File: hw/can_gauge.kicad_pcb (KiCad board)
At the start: 2 copper layers, 28 parts, among them J1 Gauge 1, J2 Gauge 2, J3 Gauge 3, J4 Gauge 4, J5 Gauge 5, J6 Gauge 6, J7 Power & CAN, U1 PIC16F1459-IP, U4 74HC595, U5 74HC595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

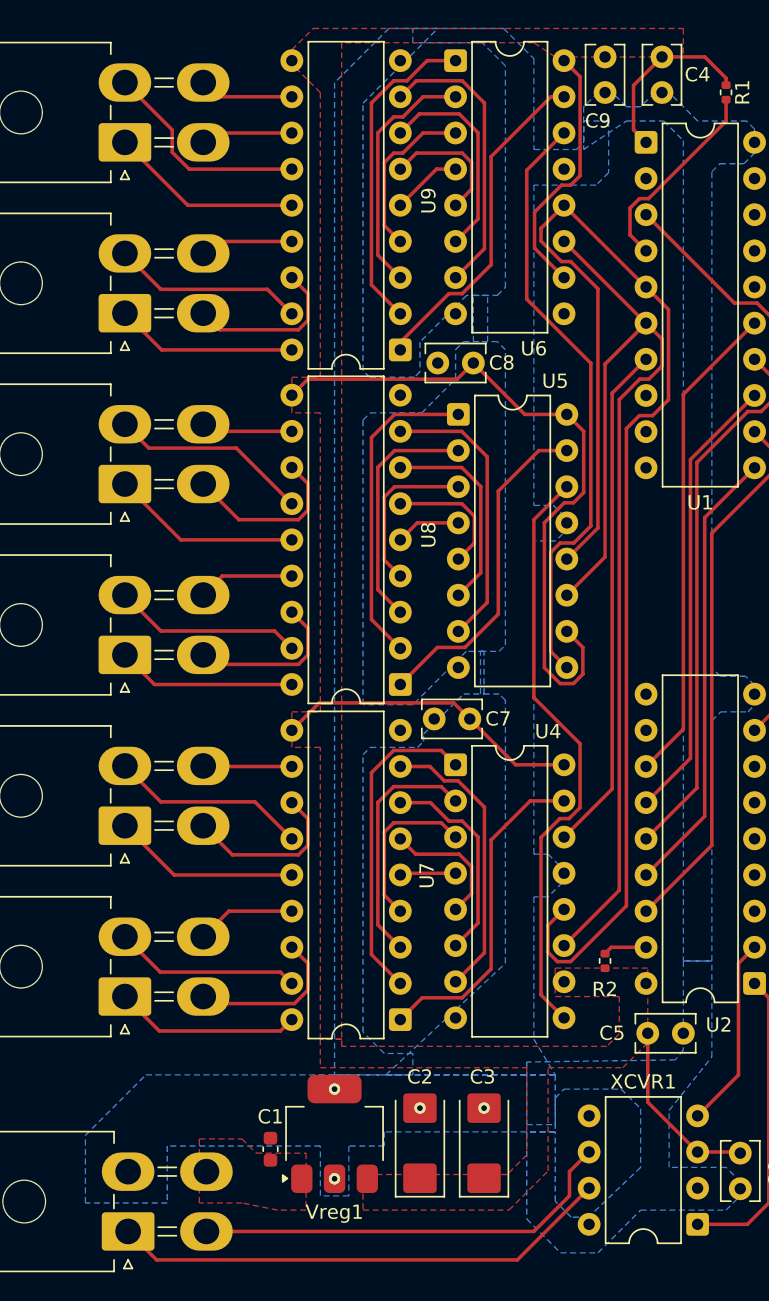
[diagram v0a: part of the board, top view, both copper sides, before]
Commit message: hw: power supply vias
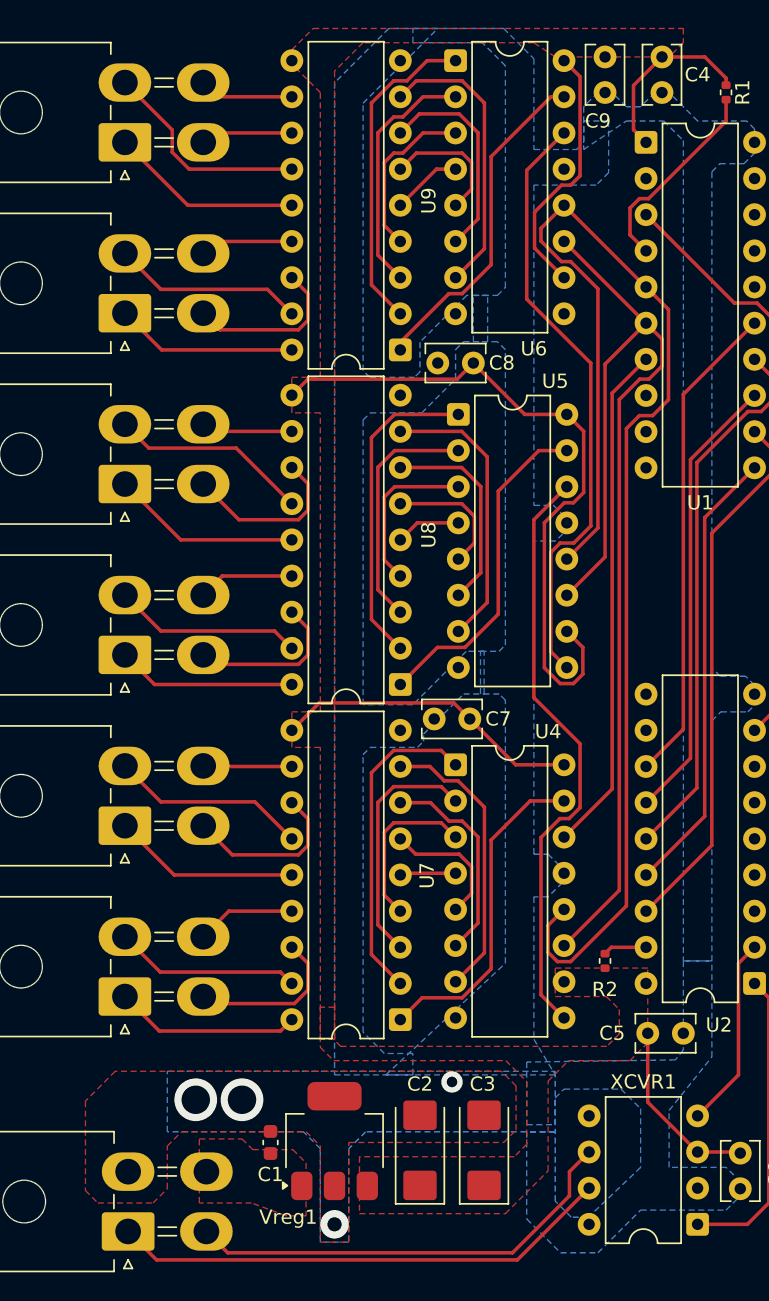
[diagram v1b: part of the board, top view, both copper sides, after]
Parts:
- moved C2 0.50 mm to (73.0, 150.3)
- moved C3 0.50 mm to (77.5, 150.3)
- moved Vreg1 0.50 mm to (67.0, 149.7)
- moved C1 0.47 mm to (62.5, 149.8)
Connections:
- Vreg1 pad 4: (no net) -> GND
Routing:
- net CAN_L: track 30.2 -> 31.4 mm
- added copper zone on F.Cu, net GND
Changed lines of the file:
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@@
 	(footprint "Package_TO_SOT_SMD:SOT-223"
 		(layer "F.Cu")
-		(at 67 149.15 90)
+		(at 67 149.65 90)
 		(descr "module CMS SOT223 4 pins")
 		(tags "CMS SOT")
 		(property "Reference" "Vreg1"
-			(at -5.5 0 0)
+			(at -5.35 -3.25 0)
 			(layer "F.SilkS")
 			(effects
@@
 			(layers "F.Cu" "F.Mask" "F.Paste")
 			(roundrect_rratio 0.25)
+			(net 1 "GND")
 		)
 		(embedded_fonts no)
@@
 	(footprint "Capacitor_SMD:C_0603_1608Metric"
 		(layer "F.Cu")
-		(at 62.5 150.225 90)
+		(at 62.5 149.75 90)
 		(descr "Capacitor SMD 0603 (1608 Metric), square (rectangular) end terminal, IPC_7351 nominal, (Body size source: IPC-SM-782 page 76, https://www.pcb-3d.com/wordpress/wp-content/uploads/ipc-sm-782a_amendment_1_and_2.pdf), generated with kicad-footprint-generator")
 		(tags "capacitor")
 		(property "Reference" "C1"
-			(at 2.275 0 180)
+			(at -2.25 0 180)
 			(layer "F.SilkS")
 			(effects
@@
 	(footprint "Capacitor_Tantalum_SMD:CP_EIA-6032-28_Kemet-C"
 		(layer "F.Cu")
-		(at 77.5 149.8 90)
+		(at 77.5 150.3 90)
 		(descr "Tantalum Capacitor SMD Kemet-C (6032-28 Metric), IPC_7351 nominal, (Body size from: http://www.kemet.com/Lists/ProductCatalog/Attachments/253/KEM_TC101_STD.pdf), generated with kicad-footprint-generator")
 		(tags "capacitor tantalum")
@@
 	(footprint "Capacitor_Tantalum_SMD:CP_EIA-6032-28_Kemet-C"
 		(layer "F.Cu")
-		(at 73 149.8 90)
+		(at 73 150.3 90)
 		(descr "Tantalum Capacitor SMD Kemet-C (6032-28 Metric), IPC_7351 nominal, (Body size from: http://www.kemet.com/Lists/ProductCatalog/Attachments/253/KEM_TC101_STD.pdf), generated with kicad-footprint-generator")
 		(tags "capacitor tantalum")
@@
 	)
 	(via
-		(at 77.5 147.3375)
-		(size 0.8)
-		(drill 0.4)
+		(at 57.25 146.75)
+		(size 3)
+		(drill 2)
 		(layers "F.Cu" "B.Cu")
+		(free yes)
 		(net 1)
 	)
 	(via
-		(at 67 152.3)
-		(size 0.8)
-		(drill 0.4)
+		(at 67 155.5)
+		(size 2)
+		(drill 1)
 		(layers "F.Cu" "B.Cu")
+		(free yes)
 		(net 1)
 	)
 	(via
-		(at 83.315 106.23)
-		(size 0.8)
-		(drill 0.4)
+		(at 60.5 146.75)
+		(size 3)
+		(drill 2)
 		(layers "F.Cu" "B.Cu")
+		(free yes)
 		(net 1)
 	)
 	(via
-		(at 67 146)
+		(at 83.315 106.23)
 		(size 0.8)
 		(drill 0.4)
 		(layers "F.Cu" "B.Cu")
-		(free yes)
 		(net 1)
 	)
 	(via
-		(at 73 147.3375)
-		(size 0.8)
-		(drill 0.4)
+		(at 75.25 145.5)
+		(size 1.5)
+		(drill 0.75)
 		(layers "F.Cu" "B.Cu")
+		(free yes)
 		(net 1)
 	)
@@
 	)
 	(segment
-		(start 58 156)
-		(end 81 156)
-		(width 0.25)
-		(layer "F.Cu")
-		(net 29)
-	)
-	(segment
-		(start 81 156)
+		(start 79.5 157.5)
 		(end 83.5 153.5)
 		(width 0.25)
@@
 	)
 	(segment
+		(start 58 156)
+		(end 59.5 157.5)
+		(width 0.25)
+		(layer "F.Cu")
+		(net 29)
+	)
+	(segment
+		(start 59.5 157.5)
+		(end 79.5 157.5)
+		(width 0.25)
+		(layer "F.Cu")
+		(net 29)
+	)
+	(segment
 		(start 88.413595 83.454)
 		(end 89.058405 83.454)
@@
 		(polygon
 			(pts
-				(xy 57.5 149.5) (xy 60.5 149.5) (xy 61.5 150.5) (xy 63.5 150.5) (xy 65 150.5) (xy 65 154.5) (xy 63 154.5)
-				(xy 60.5 154) (xy 57.5 154)
+				(xy 57.5 149.5) (xy 60.5 149.5) (xy 61.25 150.25) (xy 64.0625 150.25) (xy 65 151.1875) (xy 65 154.899999)
+				(xy 63.596206 154.899999) (xy 61.173136 154) (xy 57.5 154)
+			)
+		)
+	)
+	(zone
+		(net 1)
+		(net_name "GND")
+		(layer "F.Cu")
+		(hatch edge 0.5)
+		(priority 8)
+		(connect_pads
+			(clearance 0.5)
+		)
+		(min_thickness 0.25)
+		(filled_areas_thickness no)
+		(fill yes
+			(thermal_gap 0.5)
+			(thermal_bridge_width 0.5)
+		)
+		(polygon
+			(pts
+				(xy 66 156.75) (xy 68 156.75) (xy 68 149.75) (xy 78.875 149.75) (xy 79.75 148.875) (xy 79.75 145.78125)
+				(xy 78.71875 144.75) (xy 51.59375 144.75) (xy 49.5 146.84375) (xy 49.5 153.125) (xy 50.375 154)
+				(xy 54.25 154) (xy 55.25 153) (xy 55.25 150) (xy 56.25 149) (xy 65 149) (xy 66 150)
 			)
 		)
@@
 		(polygon
 			(pts
-				(xy 67.5 143) (xy 67.5 142.5) (xy 66 142.5) (xy 66 144.5) (xy 80.5 144.5) (xy 80.5 150.625) (xy 79.125 152)
-				(xy 69 152) (xy 69 154.5) (xy 79.25 154.5) (xy 82 151.75) (xy 82 144.5) (xy 87.25 144.5) (xy 89 142.75)
-				(xy 89 137.5) (xy 82.5 137.5) (xy 82.5 139.5) (xy 87 139.5) (xy 87 142.125) (xy 86.125 143) (xy 82 143)
+				(xy 67.4375 143) (xy 67 142.5625) (xy 67 140.25) (xy 66 140.25) (xy 66 143.0625) (xy 66.9375 144)
+				(xy 79.03125 144) (xy 80.5 145.46875) (xy 80.5 149.875) (xy 79.625 150.75) (xy 68.75 150.75) (xy 68.75 154.75)
+				(xy 79 154.75) (xy 82 151.75) (xy 82 145.4375) (xy 83.4375 144) (xy 87.75 144) (xy 89 142.75) (xy 89 137.5)
+				(xy 82.5 137.5) (xy 82.5 139.5) (xy 86.09375 139.5) (xy 87 140.40625) (xy 87 142.125) (xy 86.125 143)
+				(xy 82 143)
 			)
 		)
@@
 		(polygon
 			(pts
-				(xy 64 73) (xy 65.5 71.5) (xy 91.5 71.5) (xy 91.5 73.5) (xy 82.5 73.5) (xy 81 72.5) (xy 67.5 72.5)
-				(xy 67.5 142.5) (xy 66 142.5) (xy 66 122) (xy 64 122) (xy 64 119.5) (xy 66 119.5) (xy 66 98.5) (xy 64 98.5)
-				(xy 64 96) (xy 66 96) (xy 66 76) (xy 64 74)
+				(xy 64 73) (xy 65.5 71.5) (xy 91.5 71.5) (xy 91.5 72.5) (xy 90.5 73.5) (xy 82.5 73.5) (xy 81 72.5)
+				(xy 69 72.5) (xy 67 74.5) (xy 67 142.5) (xy 66 142.5) (xy 66 122) (xy 64 122) (xy 64 119.5) (xy 66 119.5)
+				(xy 66 98.5) (xy 64 98.5) (xy 64 96) (xy 66 96) (xy 66 76) (xy 64 74)
 			)
 		)
@@
 		(polygon
 			(pts
-				(xy 55.25 150) (xy 55.25 154) (xy 49.5 154) (xy 49.5 149.25) (xy 53.75 145) (xy 82.5 145) (xy 82.5 149)
-				(xy 70.5 149) (xy 70.5 150) (xy 68 150) (xy 68 153.5) (xy 66 153.5) (xy 66 150)
+				(xy 69.1875 149) (xy 68 150.1875) (xy 68 156.75) (xy 66 156.75) (xy 66 150.1875) (xy 64.8125 149)
+				(xy 55.25 149) (xy 55.25 144.75) (xy 82.5 144.75) (xy 82.5 149)
 			)
 		)

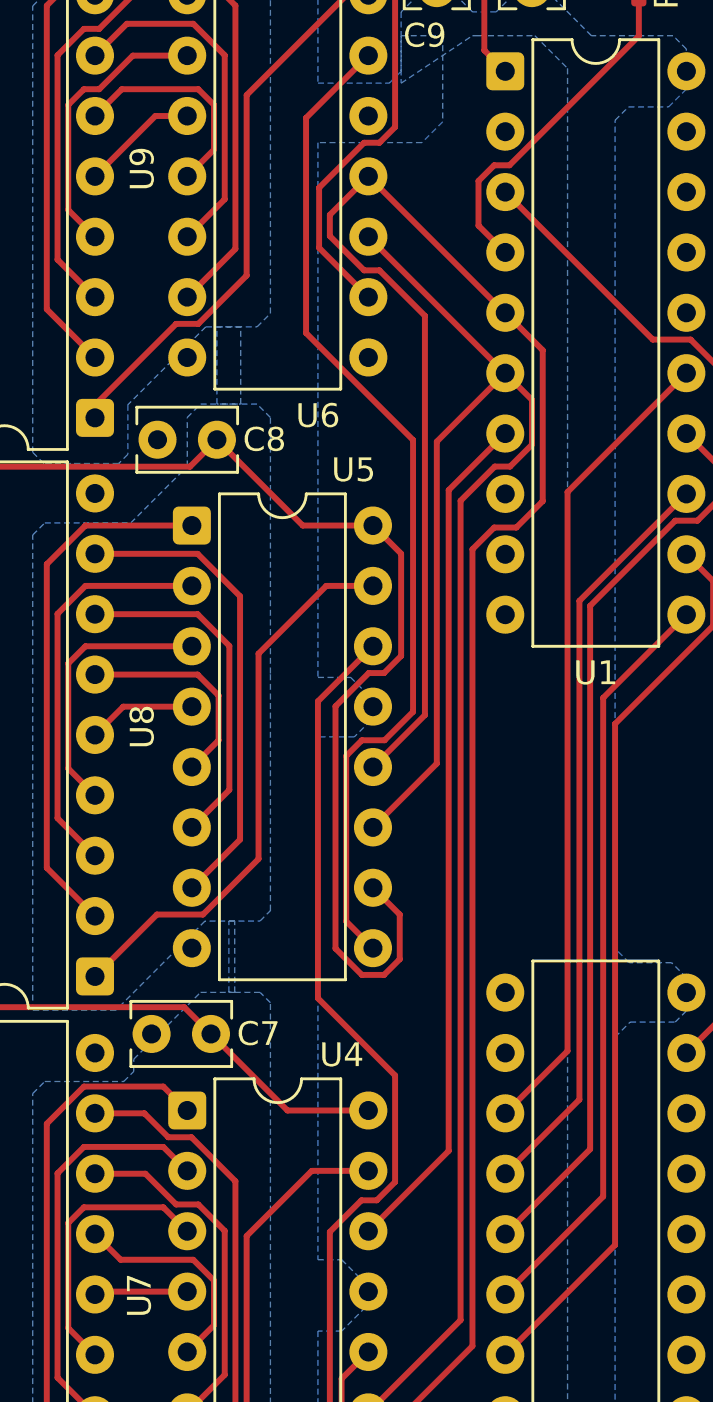
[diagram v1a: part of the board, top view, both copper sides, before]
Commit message: hw: remove redundant via
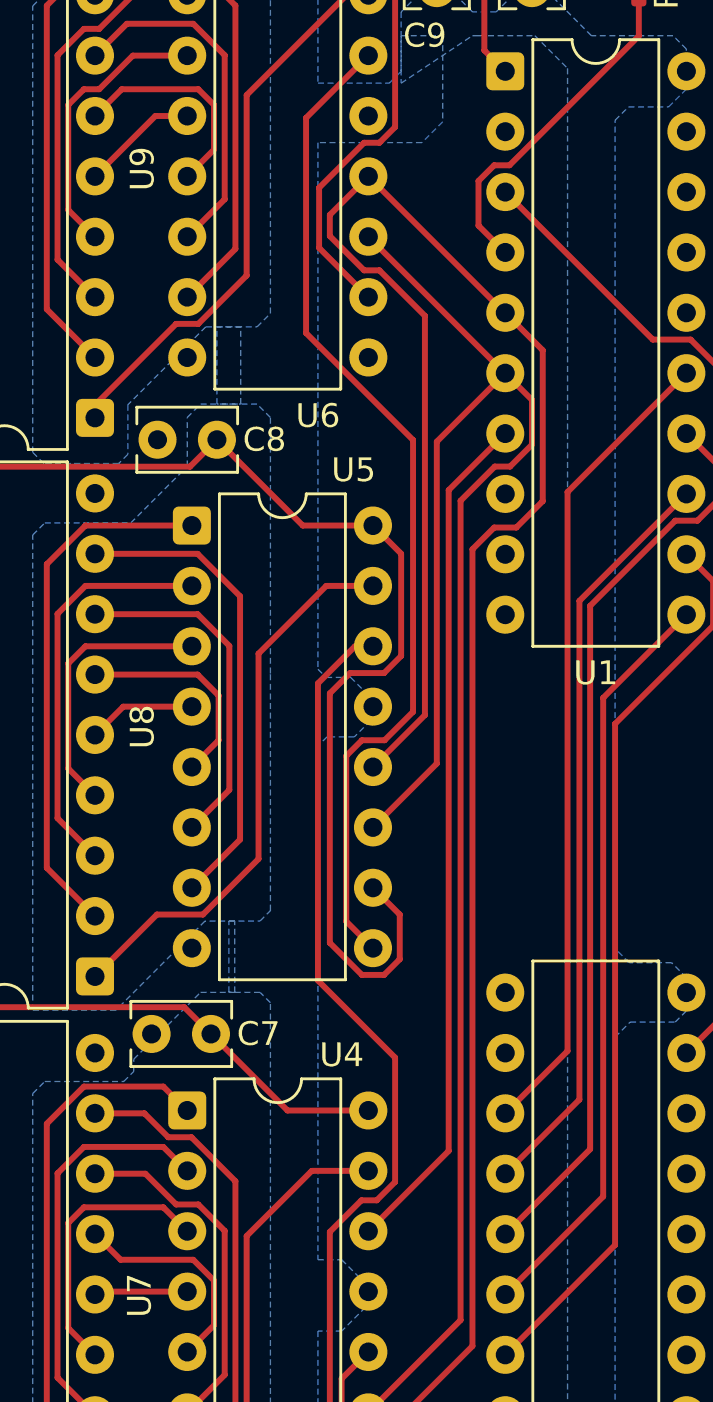
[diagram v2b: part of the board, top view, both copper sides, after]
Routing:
- net +5V: track 114.4 -> 115.1 mm
- net GND: vias 5 -> 4
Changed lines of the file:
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@@
-	)
-	(via
-		(at 83.315 106.23)
-		(size 0.8)
-		(drill 0.4)
-		(layers "F.Cu" "B.Cu")
-		(net 1)
 	)
 	(via
@@
 	)
 	(segment
-		(start 82.848595 117.516)
-		(end 81.738 116.405405)
-		(width 0.25)
-		(layer "F.Cu")
-		(net 3)
-	)
-	(segment
 		(start 83.315 98.61)
 		(end 80.36 98.61)
@@
 	)
 	(segment
+		(start 84.5 99.795)
+		(end 83.315 98.61)
+		(width 0.25)
+		(layer "F.Cu")
+		(net 3)
+	)
+	(segment
 		(start 65.126 96.134)
 		(end 64 97.26)
@@
 	)
 	(segment
-		(start 81.738 116.405405)
-		(end 81.738 106.214595)
-		(width 0.25)
-		(layer "F.Cu")
-		(net 3)
-	)
-	(segment
-		(start 83.136595 104.816)
-		(end 83.781405 104.816)
+		(start 82.848595 117.516)
+		(end 81.5 116.167405)
 		(width 0.25)
 		(layer "F.Cu")
@@
 	)
 	(segment
+		(start 84.5 104.097405)
+		(end 84.5 99.795)
+		(width 0.25)
+		(layer "F.Cu")
+		(net 3)
+	)
+	(segment
 		(start 82.941595 82.506)
 		(end 83.586405 82.506)
@@
 	)
 	(segment
+		(start 84.441 116.856405)
+		(end 83.781405 117.516)
+		(width 0.25)
+		(layer "F.Cu")
+		(net 3)
+	)
+	(segment
 		(start 81.049 84.398595)
 		(end 82.941595 82.506)
@@
 	)
 	(segment
-		(start 84.5 99.795)
-		(end 83.315 98.61)
+		(start 65.926 118.874)
+		(end 64 120.8)
+		(width 0.25)
+		(layer "F.Cu")
+		(net 3)
+	)
+	(segment
+		(start 81.049 86.929)
+		(end 81.049 84.398595)
+		(width 0.25)
+		(layer "F.Cu")
+		(net 3)
+	)
+	(segment
+		(start 83.781405 117.516)
+		(end 82.848595 117.516)
+		(width 0.25)
+		(layer "F.Cu")
+		(net 3)
+	)
+	(segment
+		(start 81.5 116.167405)
+		(end 81.5 105.671588)
+		(width 0.25)
+		(layer "F.Cu")
+		(net 3)
+	)
+	(segment
+		(start 84.441 114.976)
+		(end 84.441 116.856405)
+		(width 0.25)
+		(layer "F.Cu")
+		(net 3)
+	)
+	(segment
+		(start 83.12 89)
+		(end 81.049 86.929)
+		(width 0.25)
+		(layer "F.Cu")
+		(net 3)
+	)
+	(segment
+		(start 83.315 113.85)
+		(end 84.441 114.976)
 		(width 0.25)
 		(layer "F.Cu")
@@
 	)
 	(segment
-		(start 83.315 113.85)
-		(end 84.441 114.976)
-		(width 0.25)
-		(layer "F.Cu")
-		(net 3)
-	)
-	(segment
-		(start 84.441 114.976)
-		(end 84.441 116.856405)
-		(width 0.25)
-		(layer "F.Cu")
-		(net 3)
-	)
-	(segment
-		(start 65.926 118.874)
-		(end 64 120.8)
-		(width 0.25)
-		(layer "F.Cu")
-		(net 3)
-	)
-	(segment
-		(start 81.049 86.929)
-		(end 81.049 84.398595)
-		(width 0.25)
-		(layer "F.Cu")
-		(net 3)
-	)
-	(segment
-		(start 83.12 89)
-		(end 81.049 86.929)
+		(start 82.355588 104.816)
+		(end 83.781405 104.816)
 		(width 0.25)
 		(layer "F.Cu")
@@
 	)
 	(segment
+		(start 81.5 105.671588)
+		(end 82.355588 104.816)
+		(width 0.25)
+		(layer "F.Cu")
+		(net 3)
+	)
+	(segment
 		(start 93.01 73.5)
 		(end 94.5 74.99)
@@
 	)
 	(segment
-		(start 84.5 104.097405)
-		(end 84.5 99.795)
-		(width 0.25)
-		(layer "F.Cu")
-		(net 3)
-	)
-	(segment
-		(start 81.738 106.214595)
-		(end 83.136595 104.816)
-		(width 0.25)
-		(layer "F.Cu")
-		(net 3)
-	)
-	(segment
 		(start 92.5 150.42)
 		(end 89 146.92)
@@
 	)
 	(segment
-		(start 84.441 116.856405)
-		(end 83.781405 117.516)
-		(width 0.25)
-		(layer "F.Cu")
-		(net 3)
-	)
-	(segment
-		(start 83.781405 117.516)
-		(end 82.848595 117.516)
-		(width 0.25)
-		(layer "F.Cu")
-		(net 3)
-	)
-	(segment
 		(start 64 138.58)
 		(end 63.200001 137.780001)
@@
 	)
 	(segment
+		(start 81.5 128.327595)
+		(end 82.827595 127)
+		(width 0.25)
+		(layer "F.Cu")
+		(net 62)
+	)
+	(segment
+		(start 83.472405 127)
+		(end 84.246 126.226405)
+		(width 0.25)
+		(layer "F.Cu")
+		(net 62)
+	)
+	(segment
+		(start 83.12 141)
+		(end 81.5 139.38)
+		(width 0.25)
+		(layer "F.Cu")
+		(net 62)
+	)
+	(segment
+		(start 82.56 103.69)
+		(end 83.315 103.69)
+		(width 0.25)
+		(layer "F.Cu")
+		(net 62)
+	)
+	(segment
+		(start 81 117.75)
+		(end 81 105.25)
+		(width 0.25)
+		(layer "F.Cu")
+		(net 62)
+	)
+	(segment
+		(start 84.246 120.996)
+		(end 81 117.75)
+		(width 0.25)
+		(layer "F.Cu")
+		(net 62)
+	)
+	(segment
+		(start 81 105.25)
+		(end 82.56 103.69)
+		(width 0.25)
+		(layer "F.Cu")
+		(net 62)
+	)
+	(segment
 		(start 84.246 126.226405)
-		(end 84.246 121.746)
+		(end 84.246 120.996)
+		(width 0.25)
+		(layer "F.Cu")
+		(net 62)
+	)
+	(segment
+		(start 81.5 139.38)
+		(end 81.5 128.327595)
 		(width 0.25)
 		(layer "F.Cu")
@@
 		(start 82.827595 127)
 		(end 83.472405 127)
-		(width 0.25)
-		(layer "F.Cu")
-		(net 62)
-	)
-	(segment
-		(start 83.12 141)
-		(end 81.5 139.38)
-		(width 0.25)
-		(layer "F.Cu")
-		(net 62)
-	)
-	(segment
-		(start 84.246 121.746)
-		(end 81 118.5)
-		(width 0.25)
-		(layer "F.Cu")
-		(net 62)
-	)
-	(segment
-		(start 81 118.5)
-		(end 81 106.005)
-		(width 0.25)
-		(layer "F.Cu")
-		(net 62)
-	)
-	(segment
-		(start 81.5 139.38)
-		(end 81.5 128.327595)
-		(width 0.25)
-		(layer "F.Cu")
-		(net 62)
-	)
-	(segment
-		(start 81 106.005)
-		(end 83.315 103.69)
-		(width 0.25)
-		(layer "F.Cu")
-		(net 62)
-	)
-	(segment
-		(start 83.472405 127)
-		(end 84.246 126.226405)
-		(width 0.25)
-		(layer "F.Cu")
-		(net 62)
-	)
-	(segment
-		(start 81.5 128.327595)
-		(end 82.827595 127)
 		(width 0.25)
 		(layer "F.Cu")
@@
 				(xy 76.75 90.25) (xy 78.4375 90.25) (xy 79 89.6875) (xy 79 74.125) (xy 77.375 72.5) (xy 72.5 72.5)
 				(xy 72.5 71.5) (xy 78.875 71.5) (xy 81 73.625) (xy 81 80) (xy 84 80) (xy 84.5 79.5) (xy 84.5 78)
-				(xy 86.25 78) (xy 86.25 81.625) (xy 85.375 82.5) (xy 81 82.5) (xy 81 105) (xy 82.375 105) (xy 83.5 106.125)
-				(xy 83.5 106.53125) (xy 82.53125 107.5) (xy 81 107.5) (xy 81 129.5) (xy 82 129.5) (xy 83 130.5)
-				(xy 83 131.5) (xy 82 132.5) (xy 81 132.5) (xy 81 142.5) (xy 82.5 145)
+				(xy 86.25 78) (xy 86.25 81.625) (xy 85.375 82.5) (xy 81 82.5) (xy 81 104.65625) (xy 81.34375 105)
+				(xy 82.375 105) (xy 83.5 106.125) (xy 83.5 106.53125) (xy 82.53125 107.5) (xy 81.382812 107.5) (xy 81 107.882812)
+				(xy 81 129.5) (xy 82 129.5) (xy 83 130.5) (xy 83 131.5) (xy 82 132.5) (xy 81 132.5) (xy 81 142.5)
+				(xy 82.5 145)
 			)
 		)

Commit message: hw: fix errors
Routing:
- net +5V: track 115.1 -> 124.2 mm
- net GND: vias 4 -> 5
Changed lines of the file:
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@@
 		(tags "CMS SOT")
 		(property "Reference" "Vreg1"
-			(at -5.35 -3.25 0)
+			(at -6.1 3.5 0)
 			(layer "F.SilkS")
 			(effects
@@
 	)
 	(via
+		(at 54 146.75)
+		(size 3)
+		(drill 2)
+		(layers "F.Cu" "B.Cu")
+		(free yes)
+		(net 1)
+	)
+	(via
 		(at 75.25 145.5)
 		(size 1.5)
@@
 	)
 	(segment
+		(start 86 137.51)
+		(end 87.81 137.51)
+		(width 0.25)
+		(layer "F.Cu")
+		(net 3)
+	)
+	(segment
 		(start 82.941595 82.506)
 		(end 83.586405 82.506)
@@
 	)
 	(segment
+		(start 83.12 138.46)
+		(end 88.76 138.46)
+		(width 0.25)
+		(layer "F.Cu")
+		(net 3)
+	)
+	(segment
 		(start 75.616 96.134)
 		(end 65.126 96.134)
@@
 	)
 	(segment
+		(start 88.76 138.46)
+		(end 88.88 138.58)
+		(width 0.25)
+		(layer "F.Cu")
+		(net 3)
+	)
+	(segment
 		(start 82.355588 104.816)
 		(end 83.781405 104.816)
@@
 	)
 	(segment
+		(start 87.81 137.51)
+		(end 88.88 138.58)
+		(width 0.25)
+		(layer "F.Cu")
+		(net 3)
+	)
+	(segment
 		(start 64 138.58)
 		(end 63.200001 137.780001)
@@
 				(xy 79.03125 144) (xy 80.5 145.46875) (xy 80.5 149.875) (xy 79.625 150.75) (xy 68.75 150.75) (xy 68.75 154.75)
 				(xy 79 154.75) (xy 82 151.75) (xy 82 145.4375) (xy 83.4375 144) (xy 87.75 144) (xy 89 142.75) (xy 89 137.5)
-				(xy 82.5 137.5) (xy 82.5 139.5) (xy 86.09375 139.5) (xy 87 140.40625) (xy 87 142.125) (xy 86.125 143)
-				(xy 82 143)
+				(xy 87 137.5) (xy 87 142.125) (xy 86.125 143) (xy 82 143)
 			)
 		)
@@
 		(min_thickness 0.25)
 		(filled_areas_thickness no)
-		(fill yes
+		(fill
 			(thermal_gap 0.5)
 			(thermal_bridge_width 0.5)
@@
 			(pts
 				(xy 69.1875 149) (xy 68 150.1875) (xy 68 156.75) (xy 66 156.75) (xy 66 150.1875) (xy 64.8125 149)
-				(xy 55.25 149) (xy 55.25 144.75) (xy 82.5 144.75) (xy 82.5 149)
+				(xy 51.75 149) (xy 51.75 144.75) (xy 82.5 144.75) (xy 82.5 149)
 			)
 		)

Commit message: hw: USB port
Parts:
- added C10: 0.1 uF, Capacitor_THT:C_Rect_L4.0mm_W2.5mm_P2.50mm, F.Cu at (68.5, 172.5)
- added F1: 500 mA, Fuse:Fuse_0402_1005Metric, F.Cu at (61.0, 172.5)
- added J8: USB_B, footprints:UJ2-BH-BL1-TH, F.Cu at (53.2, 169.8)
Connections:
- U1 pad 18: unconnected-(U1-RA1/D-/ICSPCLK-Pad18) -> USB-
- U1 pad 19: unconnected-(U1-RA0/D+/ICSPDAT-Pad19) -> USB+
- Vreg1 pad 4: GND -> (no net)
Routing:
- net USB+: track 0.00 -> 127.3 mm
- net USB-: track 0.00 -> 121.1 mm
- net GND: track 0.00 -> 39.3 mm
- net Net-(J8-VBUS): track 0.00 -> 8.45 mm
- net +5V: track 124.2 -> 128.7 mm
